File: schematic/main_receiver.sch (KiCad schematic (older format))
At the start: 61 parts, among them J7 UFL, J8 raspberry_pi_3_header, U18 MAX-M8, U7 SX1301, X1 ABRACON-OSC

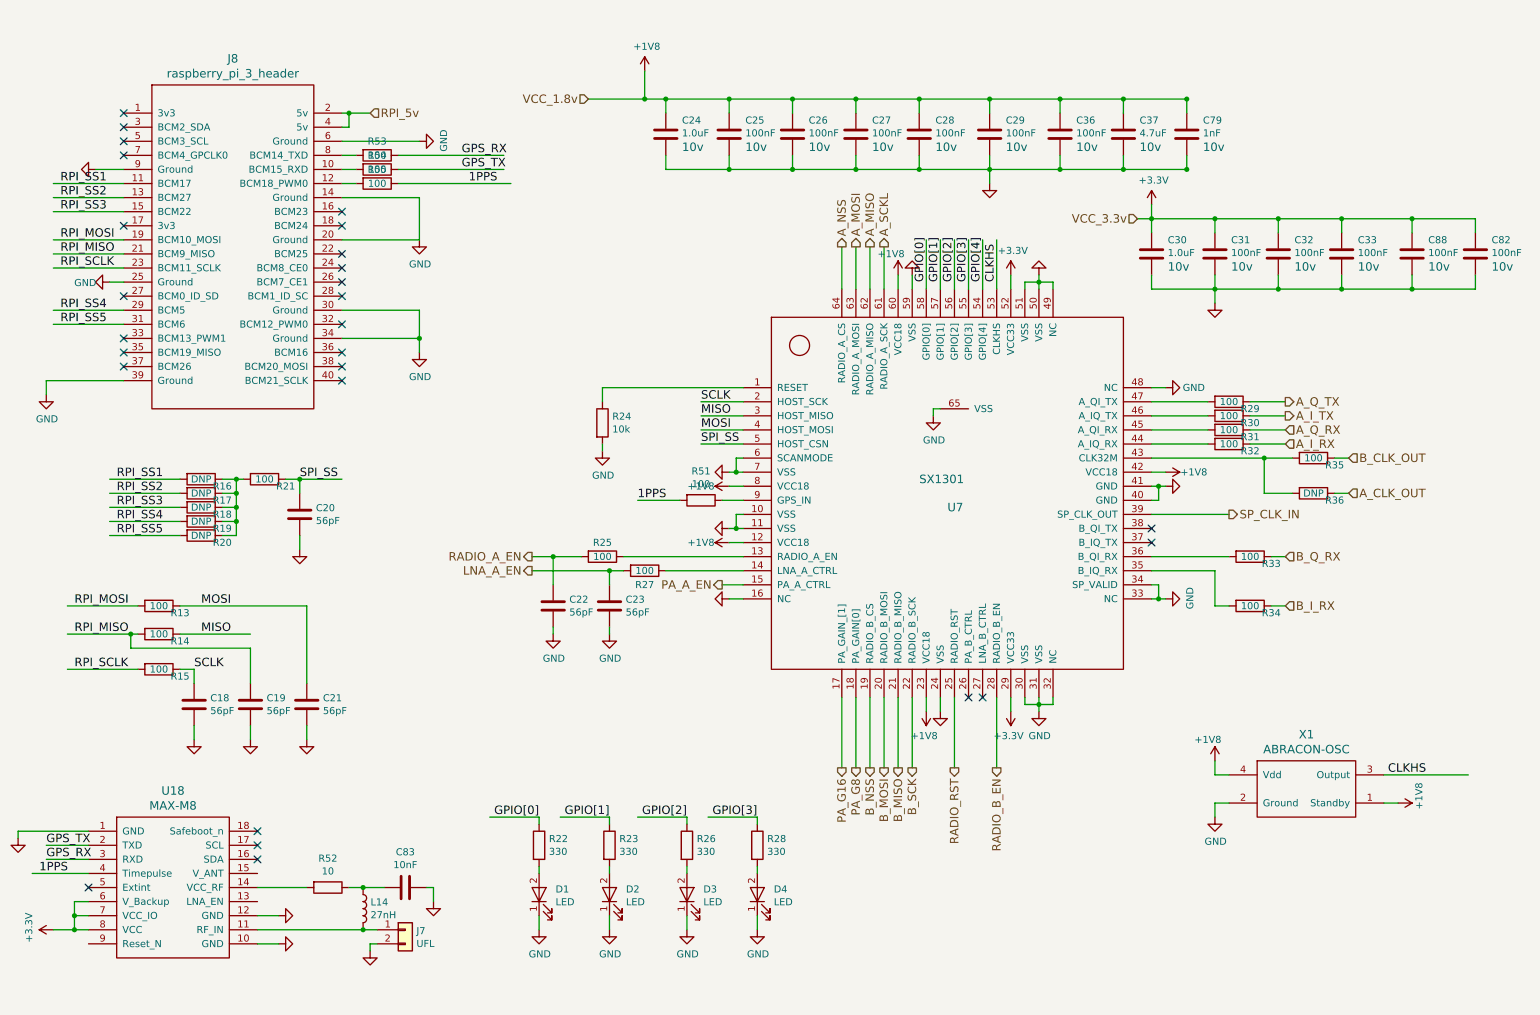
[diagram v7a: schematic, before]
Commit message: More updates to bom, added resistors to all communication lines
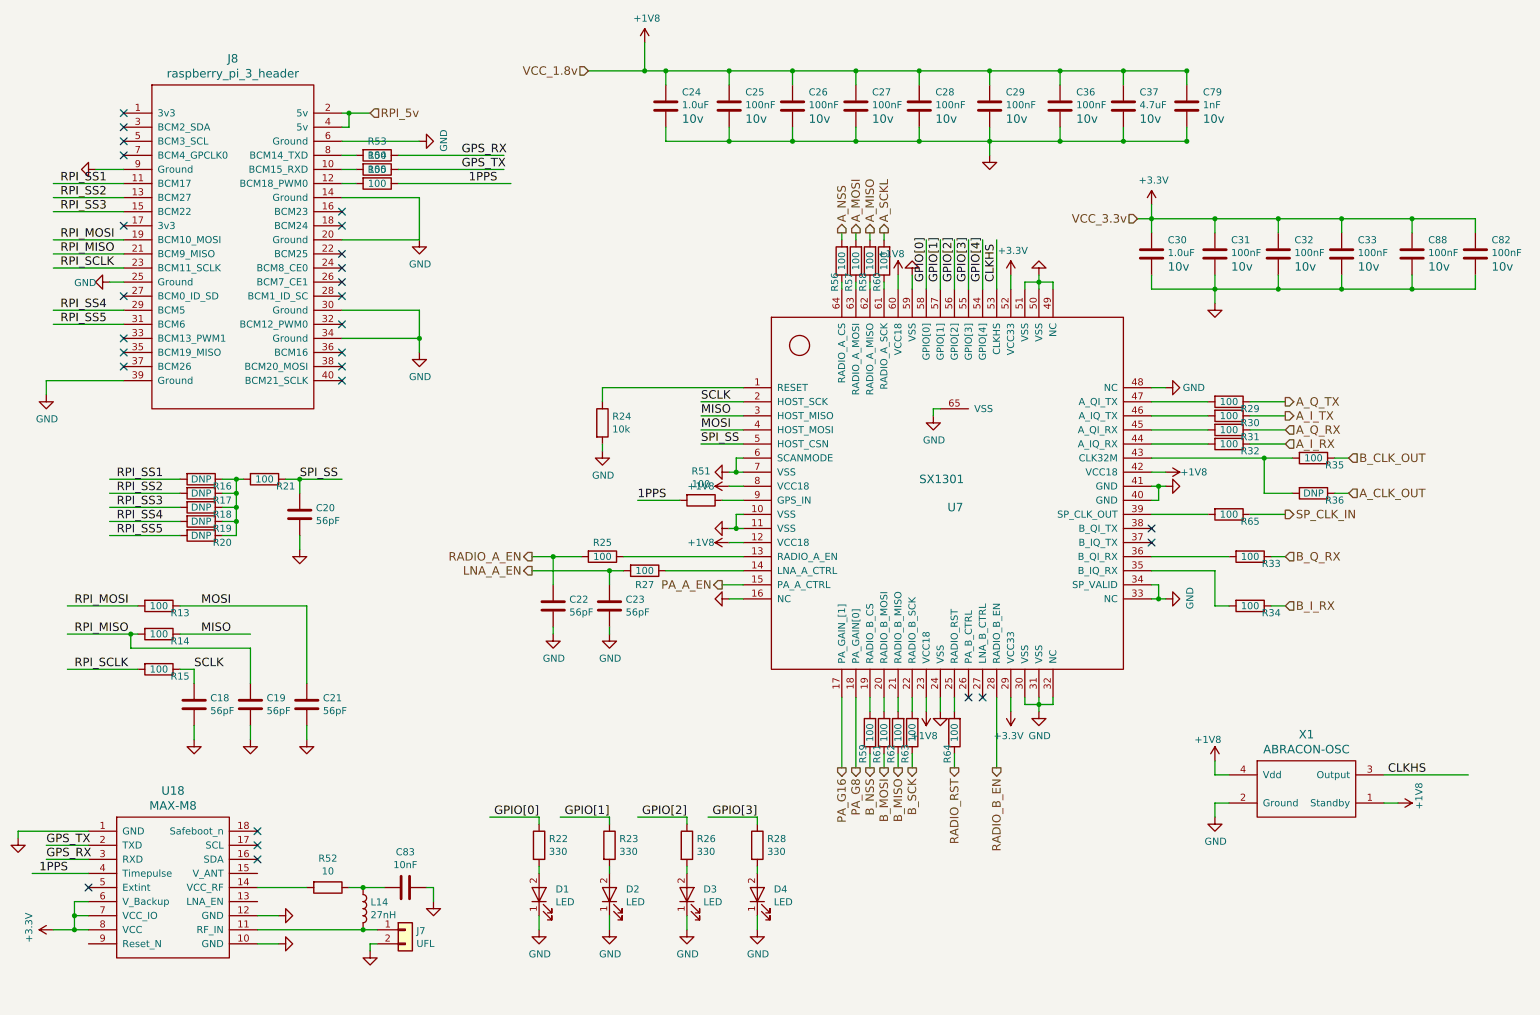
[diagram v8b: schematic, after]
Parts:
- added R56, R57, R58, R59, R60, R61, R62, R63, R64, R65: 100, Resistors_SMD:R_0402_NoSilk, symbol R
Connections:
- wire segments 220 -> 230
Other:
- moved on the sheet: C24, C25, C26, C27, C28, C29, C36, C37, C79
